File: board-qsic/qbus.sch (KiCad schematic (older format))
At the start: 63 parts, among them J301 SD Card, J302 SD Card, J501 USB_A, P501 Indicator Panel, U101 XC7A75T-CSG324, U501 MT25Q-mlq8, U502 TPS2561, U503 MAX3033E, U504 USB3340, X501 ASE-24.000MHz

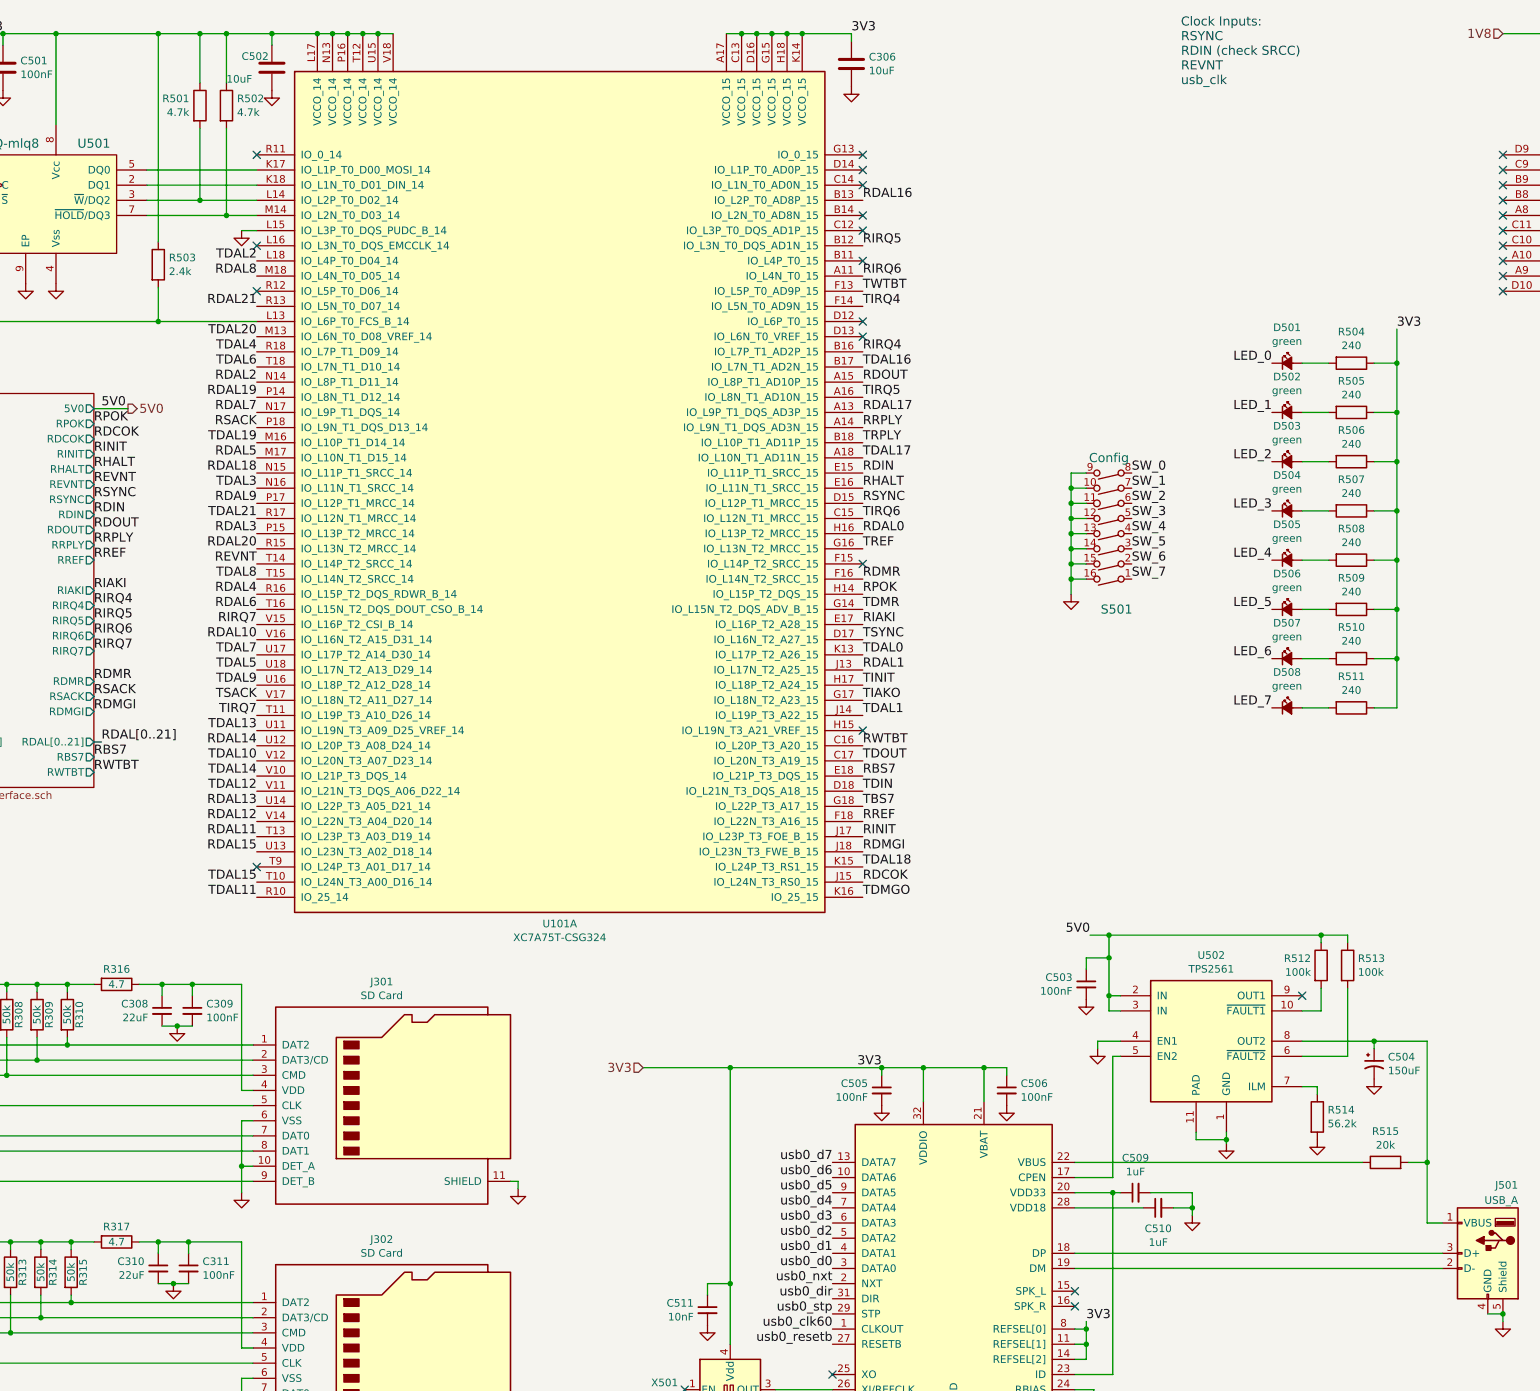
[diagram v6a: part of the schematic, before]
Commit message: These are all old changes in directories that are now historical.
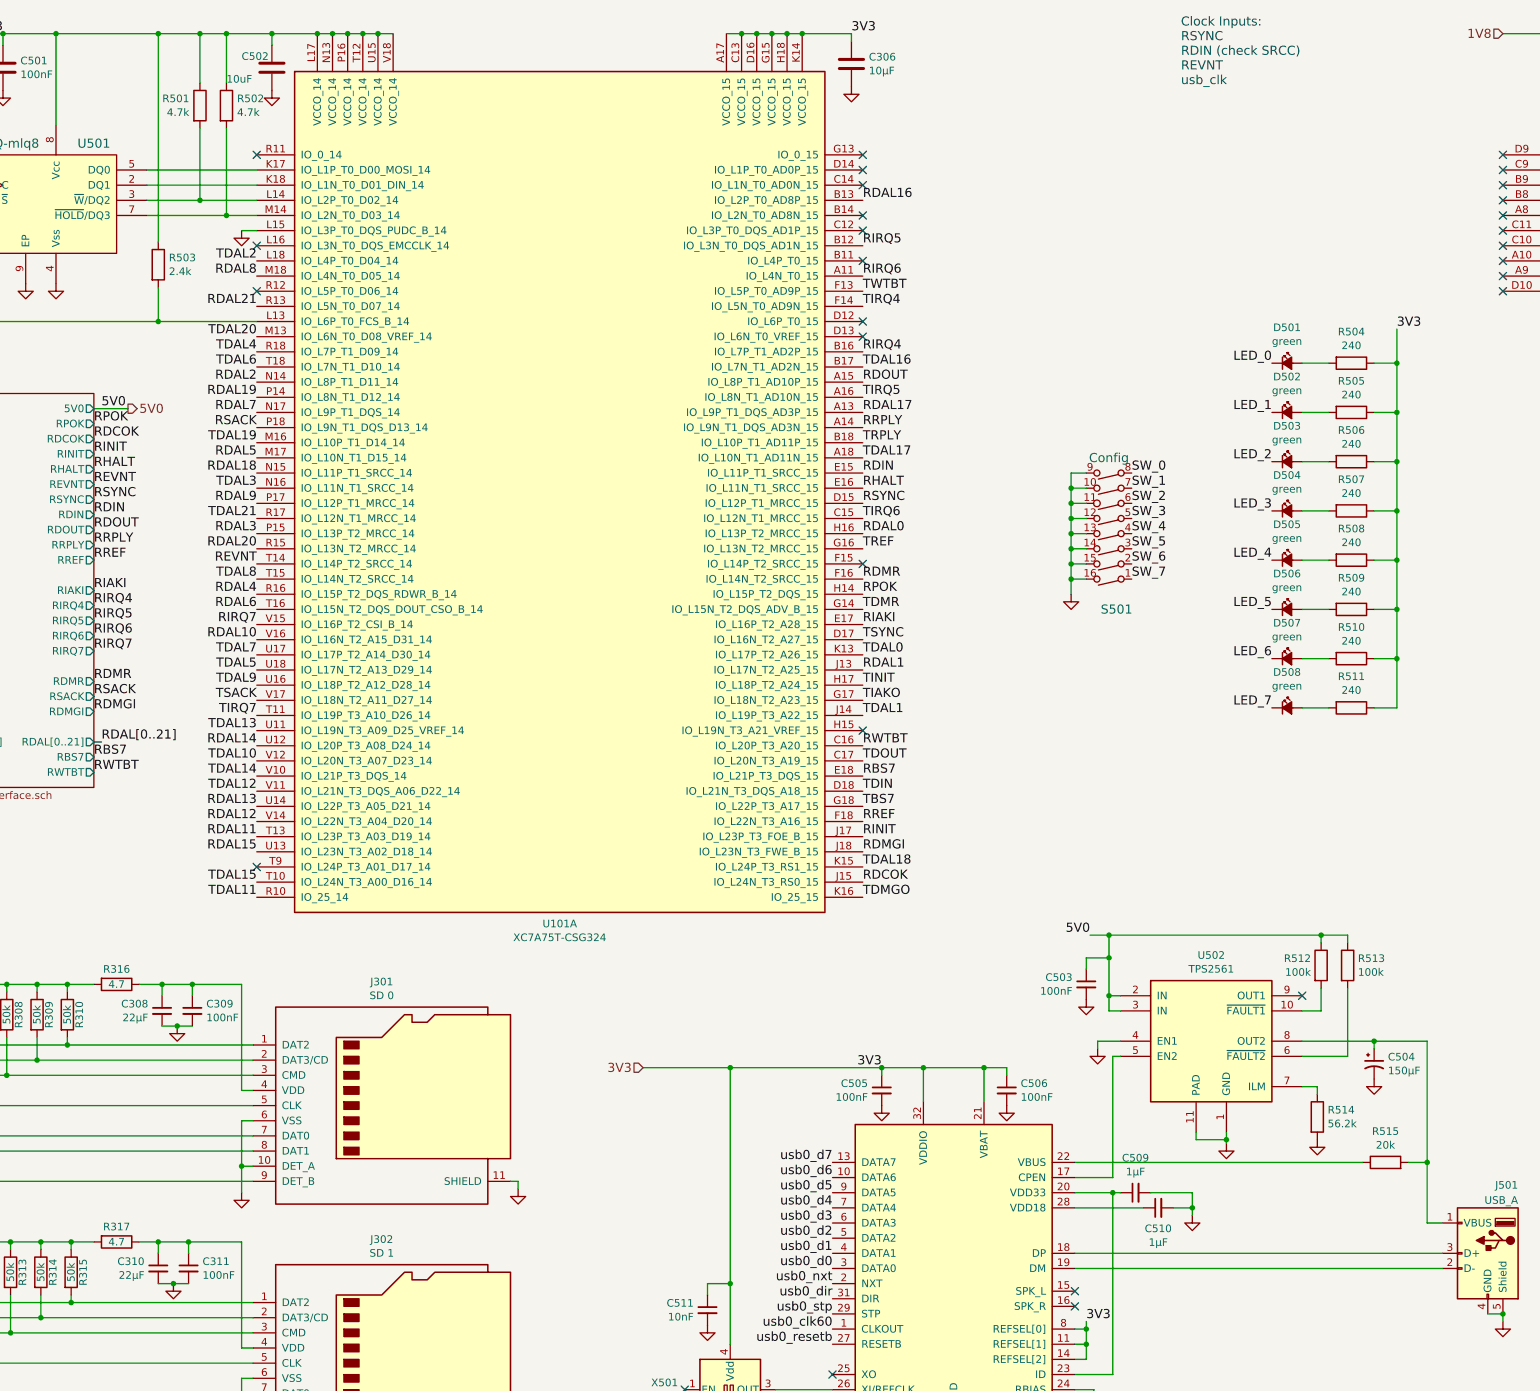
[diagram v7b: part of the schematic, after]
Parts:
- C306: value 10uF -> 10µF
- C308, C310: value 22uF -> 22µF
- C504: value 150uF -> 150µF
- C509, C510: value 1uF -> 1µF
- J301: value SD Card -> SD 0
- J302: value SD Card -> SD 1
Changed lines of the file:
@@
 AR Path="/5DA36495/5DA029C9" Ref="U?"  Part="1"
 AR Path="/5DCB8CA6/5DA029C9" Ref="U504"  Part="1"
+AR Path="/5DA029C9" Ref="U504"  Part="1"
 F 0 "U504" H 8375 7925 50  0000 C CNN
 F 1 "USB3340" H 7425 7925 50  0000 C CNN
@@
 AR Path="/5DCB8CA6/5DA02A09" Ref="C504"  Part="1"
 F 0 "C504" H 10741 7646 50  0000 L CNN
-F 1 "150uF" H 10741 7555 50  0000 L CNN
+F 1 "150µF" H 10741 7555 50  0000 L CNN
 F 2 "Capacitor_SMD:CP_Elec_6.3x5.7" H 10650 7600 50  0001 C CNN
 F 3 "~" H 10650 7600 50  0001 C CNN
@@
 AR Path="/5DCB8CA6/5DA02AFE" Ref="C509"  Part="1"
 F 0 "C509" V 9304 8450 50  0000 C CNN
-F 1 "1uF" V 9213 8450 50  0000 C CNN
+F 1 "1µF" V 9213 8450 50  0000 C CNN
 F 2 "Capacitor_SMD:C_0603_1608Metric" H 9075 8450 50  0001 C CNN
 F 3 "~" H 9075 8450 50  0001 C CNN
@@
 AR Path="/5DCB8CA6/5DA02B0A" Ref="C510"  Part="1"
 F 0 "C510" V 9088 8550 50  0000 C CNN
-F 1 "1uF" V 8997 8550 50  0000 C CNN
+F 1 "1µF" V 8997 8550 50  0000 C CNN
 F 2 "Capacitor_SMD:C_0603_1608Metric" H 9225 8550 50  0001 C CNN
 F 3 "~" H 9225 8550 50  0001 C CNN
@@
 AR Path="/5DCB8CA6/5DECE66B" Ref="J301"  Part="1"
 F 0 "J301" H 4100 8692 50  0000 C CNN
-F 1 "SD Card" H 4100 8601 50  0000 C CNN
+F 1 "SD 0" H 4100 8601 50  0000 C CNN
 F 2 "Connector_Card:microSD_HC_Hirose_DM3BT-DSF-PEJS" H 6200 8575 50  0001 C CNN
 F 3 "https://www.hirose.com/product/download/?distributor=digikey&type=2d&lang=en&num=DM3BT-DSF-PEJS" H 4150 7975 50  0001 C CNN
@@
 AR Path="/5DCB8CA6/5DEDBE60" Ref="J302"  Part="1"
 F 0 "J302" H 4100 10392 50  0000 C CNN
-F 1 "SD Card" H 4100 10301 50  0000 C CNN
+F 1 "SD 1" H 4100 10301 50  0000 C CNN
 F 2 "Connector_Card:microSD_HC_Hirose_DM3BT-DSF-PEJS" H 6200 10275 50  0001 C CNN
 F 3 "https://www.hirose.com/product/download/?distributor=digikey&type=2d&lang=en&num=DM3BT-DSF-PEJS" H 4150 9675 50  0001 C CNN
@@
 P 7200 1000
 F 0 "C306" H 7315 1046 50  0000 L CNN
-F 1 "10uF" H 7315 955 50  0000 L CNN
+F 1 "10µF" H 7315 955 50  0000 L CNN
 F 2 "Capacitor_SMD:C_0603_1608Metric" H 7238 850 50  0001 C CNN
 F 3 "~" H 7200 1000 50  0001 C CNN
@@
 AR Path="/5DCB8CA6/5DA8A5C8" Ref="C308"  Part="1"
 F 0 "C308" H 2559 7296 50  0000 R CNN
-F 1 "22uF" H 2559 7205 50  0000 R CNN
+F 1 "22µF" H 2559 7205 50  0000 R CNN
 F 2 "Capacitor_SMD:C_0805_2012Metric" H 2650 7250 50  0001 C CNN
 F 3 "~" H 2650 7250 50  0001 C CNN
@@
 AR Path="/5DCB8CA6/5DA8BA17" Ref="C310"  Part="1"
 F 0 "C310" H 2534 8996 50  0000 R CNN
-F 1 "22uF" H 2534 8905 50  0000 R CNN
+F 1 "22µF" H 2534 8905 50  0000 R CNN
 F 2 "Capacitor_SMD:C_0805_2012Metric" H 2625 8950 50  0001 C CNN
 F 3 "~" H 2625 8950 50  0001 C CNN
